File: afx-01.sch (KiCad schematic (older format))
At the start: 21 parts, among them P1 CONN_02X05, P2 CONN_02X08, Q5 BSS138, Q6 BSS138, U1 ADA_SSD1306_I2C, U10 MicroSD_Connector, U2 Teensy_3.1, U4 MicroSD_Adapter, U5 MCP1703

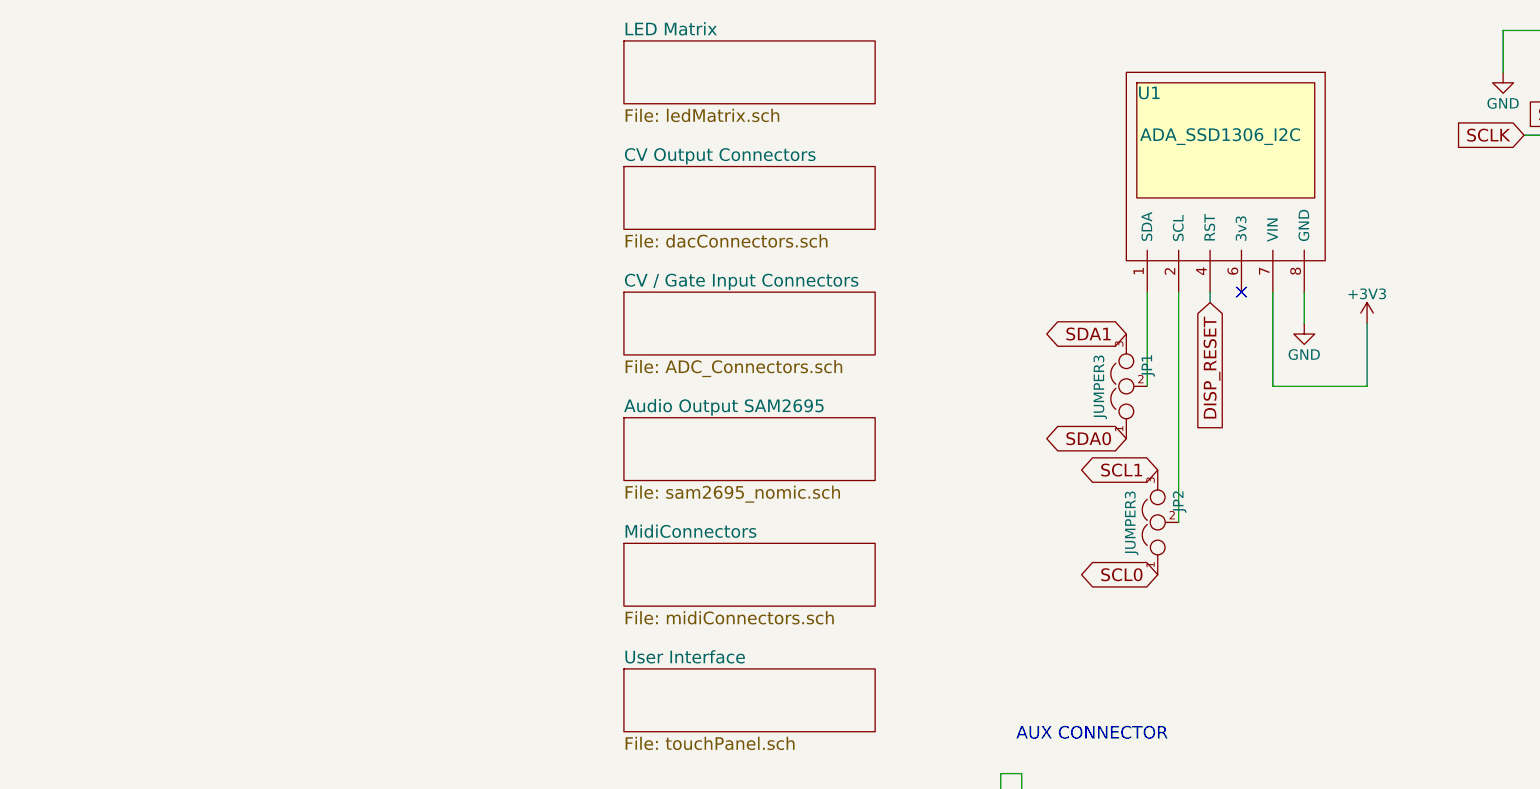
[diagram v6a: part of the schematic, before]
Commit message: UPDATING SCHEMATIC FOR SSD1327
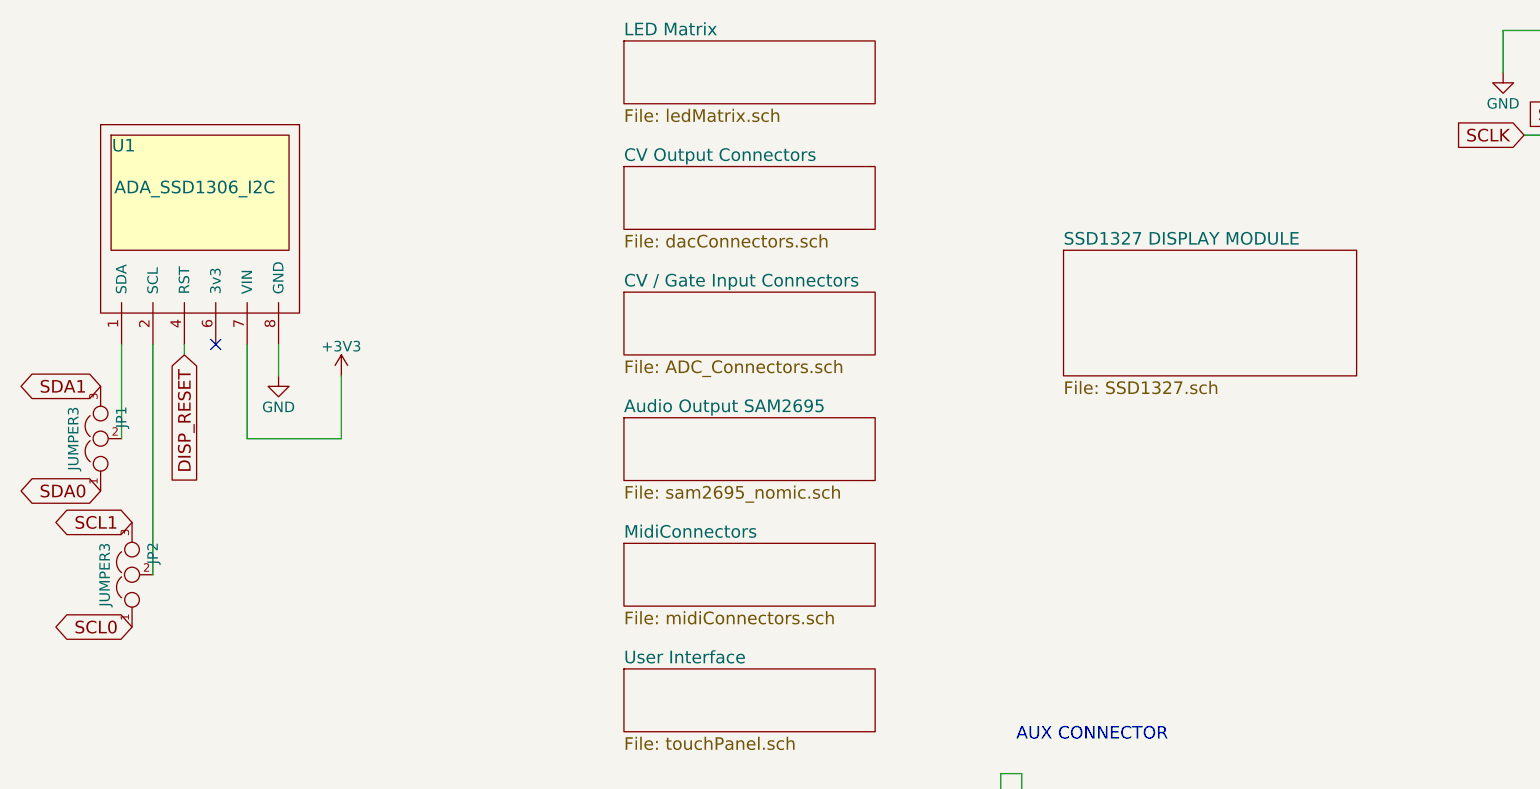
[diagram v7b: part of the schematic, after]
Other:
- moved on the sheet: JP1, JP2, U1
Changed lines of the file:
@@
 $Descr A4 11693 8268
 encoding utf-8
-Sheet 1 7
+Sheet 1 8
 Title ""
 Date ""
@@
 	0    -1   -1   0
 $EndComp
-NoConn ~ 3950 2000
+NoConn ~ -950 2250
 $Comp
 L ADA_SSD1306_I2C U1
 U 1 1 558492E1
-P 3850 1600
-F 0 "U1" H 3510 2150 60  0000 C CNN
-F 1 "ADA_SSD1306_I2C" H 3850 1950 60  0000 C CNN
-F 2 "Pin_Headers:Pin_Header_Straight_1x06" V 4050 1550 60  0001 C CNN
-F 3 "" V 4050 1550 60  0000 C CNN
-	1    3850 1600
+P -1050 1850
+F 0 "U1" H -1390 2400 60  0000 C CNN
+F 1 "ADA_SSD1306_I2C" H -1050 2200 60  0000 C CNN
+F 2 "Pin_Headers:Pin_Header_Straight_1x06" V -850 1800 60  0001 C CNN
+F 3 "" V -850 1800 60  0000 C CNN
+	1    -1050 1850
 	1    0    0    -1
 $EndComp
@@
 SD_CS
 $Comp
-L +3V3 #PWR17
+L +3V3 #PWR01
 U 1 1 561E6C12
 P 6800 5200
-F 0 "#PWR17" H 6800 5050 50  0001 C CNN
+F 0 "#PWR01" H 6800 5050 50  0001 C CNN
 F 1 "+3V3" H 6800 5340 50  0000 C CNN
 F 2 "" H 6800 5200 60  0000 C CNN
@@
 SCL1
 $Comp
-L +3V3 #PWR19
+L +3V3 #PWR02
 U 1 1 561E70C9
 P 10650 5200
-F 0 "#PWR19" H 10650 5050 50  0001 C CNN
+F 0 "#PWR02" H 10650 5050 50  0001 C CNN
 F 1 "+3V3" H 10650 5340 50  0000 C CNN
 F 2 "" H 10650 5200 60  0000 C CNN
@@
 Text GLabel 9900 3000 2    60   BiDi ~ 0
 SCL0
-Text GLabel 3400 2200 0    60   BiDi ~ 0
+Text GLabel -1500 2450 0    60   BiDi ~ 0
 SDA1
-Text GLabel 3550 2850 0    60   BiDi ~ 0
+Text GLabel -1350 3100 0    60   BiDi ~ 0
 SCL1
 Text GLabel 8600 4200 3    60   BiDi ~ 0
@@
 ENC1B
 $Comp
-L +3V3 #PWR12
+L +3V3 #PWR03
 U 1 1 561E88DC
 P 9300 3950
-F 0 "#PWR12" H 9300 3800 50  0001 C CNN
+F 0 "#PWR03" H 9300 3800 50  0001 C CNN
 F 1 "+3V3" H 9300 4090 50  0000 C CNN
 F 2 "" H 9300 3950 60  0000 C CNN
@@
 $EndComp
 $Comp
-L GND #PWR13
+L GND #PWR04
 U 1 1 561E894C
 P 9000 4050
-F 0 "#PWR13" H 9000 3800 50  0001 C CNN
+F 0 "#PWR04" H 9000 3800 50  0001 C CNN
 F 1 "GND" H 9000 3900 50  0000 C CNN
 F 2 "" H 9000 4050 60  0000 C CNN
@@
 $EndComp
 $Comp
-L +5V #PWR10
+L +5V #PWR05
 U 1 1 561E8C0A
 P 9500 2150
-F 0 "#PWR10" H 9500 2000 50  0001 C CNN
+F 0 "#PWR05" H 9500 2000 50  0001 C CNN
 F 1 "+5V" H 9500 2290 50  0000 C CNN
 F 2 "" H 9500 2150 60  0000 C CNN
@@
 $EndComp
 $Comp
-L +3V3 #PWR11
+L +3V3 #PWR06
 U 1 1 561E8F33
 P 9950 2400
-F 0 "#PWR11" H 9950 2250 50  0001 C CNN
+F 0 "#PWR06" H 9950 2250 50  0001 C CNN
 F 1 "+3V3" H 9950 2540 50  0000 C CNN
 F 2 "" H 9950 2400 60  0000 C CNN
@@
 $EndComp
 $Comp
-L GNDA #PWR7
+L GNDA #PWR07
 U 1 1 561E8FA3
 P 9800 2000
-F 0 "#PWR7" H 9800 1750 50  0001 C CNN
+F 0 "#PWR07" H 9800 1750 50  0001 C CNN
 F 1 "GNDA" H 9800 1850 50  0000 C CNN
 F 2 "" H 9800 2000 60  0000 C CNN
@@
 SCLK
 $Comp
-L GND #PWR6
+L GND #PWR08
 U 1 1 561E9F99
 P 9250 1800
-F 0 "#PWR6" H 9250 1550 50  0001 C CNN
+F 0 "#PWR08" H 9250 1550 50  0001 C CNN
 F 1 "GND" H 9250 1650 50  0000 C CNN
 F 2 "" H 9250 1800 60  0000 C CNN
@@
 $EndComp
 $Comp
-L GND #PWR5
+L GND #PWR09
 U 1 1 561EA0E7
 P 7550 1800
-F 0 "#PWR5" H 7550 1550 50  0001 C CNN
+F 0 "#PWR09" H 7550 1550 50  0001 C CNN
 F 1 "GND" H 7550 1650 50  0000 C CNN
 F 2 "" H 7550 1800 60  0000 C CNN
@@
 SCLK
 $Comp
-L GND #PWR1
+L GND #PWR010
 U 1 1 561EAAFA
 P 5200 950
-F 0 "#PWR1" H 5200 700 50  0001 C CNN
+F 0 "#PWR010" H 5200 700 50  0001 C CNN
 F 1 "GND" H 5200 800 50  0000 C CNN
 F 2 "" H 5200 950 60  0000 C CNN
@@
 MOSI
 $Comp
-L +5V #PWR4
+L +5V #PWR011
 U 1 1 561EAD75
 P 6950 1600
-F 0 "#PWR4" H 6950 1450 50  0001 C CNN
+F 0 "#PWR011" H 6950 1450 50  0001 C CNN
 F 1 "+5V" H 6950 1740 50  0000 C CNN
 F 2 "" H 6950 1600 60  0000 C CNN
@@
 Text GLabel 6650 2900 0    60   Output ~ 0
 DISP_RESET
-Text GLabel 3800 2050 3    60   Input ~ 0
+Text GLabel -1100 2300 3    60   Input ~ 0
 DISP_RESET
 $Comp
-L GND #PWR8
+L GND #PWR012
 U 1 1 561EB8E2
-P 4250 2150
-F 0 "#PWR8" H 4250 1900 50  0001 C CNN
-F 1 "GND" H 4250 2000 50  0000 C CNN
-F 2 "" H 4250 2150 60  0000 C CNN
-F 3 "" H 4250 2150 60  0000 C CNN
-	1    4250 2150
-	1    0    0    -1
-$EndComp
-$Comp
-L +3V3 #PWR9
+P -650 2400
+F 0 "#PWR012" H -650 2150 50  0001 C CNN
+F 1 "GND" H -650 2250 50  0000 C CNN
+F 2 "" H -650 2400 60  0000 C CNN
+F 3 "" H -650 2400 60  0000 C CNN
+	1    -650 2400
+	1    0    0    -1
+$EndComp
+$Comp
+L +3V3 #PWR013
 U 1 1 561EBA2E
-P 4550 2150
-F 0 "#PWR9" H 4550 2000 50  0001 C CNN
-F 1 "+3V3" H 4550 2290 50  0000 C CNN
-F 2 "" H 4550 2150 60  0000 C CNN
-F 3 "" H 4550 2150 60  0000 C CNN
-	1    4550 2150
+P -350 2400
+F 0 "#PWR013" H -350 2250 50  0001 C CNN
+F 1 "+3V3" H -350 2540 50  0000 C CNN
+F 2 "" H -350 2400 60  0000 C CNN
+F 3 "" H -350 2400 60  0000 C CNN
+	1    -350 2400
 	1    0    0    -1
 $EndComp
@@
 LED_DIN
 $Comp
-L GND #PWR14
+L GND #PWR014
 U 1 1 561EC8D9
 P 2800 4400
-F 0 "#PWR14" H 2800 4150 50  0001 C CNN
+F 0 "#PWR014" H 2800 4150 50  0001 C CNN
 F 1 "GND" H 2800 4250 50  0000 C CNN
 F 2 "" H 2800 4400 60  0000 C CNN
@@
 $EndComp
 $Comp
-L +3V3 #PWR15
+L +3V3 #PWR015
 U 1 1 561EC92C
 P 2550 4550
-F 0 "#PWR15" H 2550 4400 50  0001 C CNN
+F 0 "#PWR015" H 2550 4400 50  0001 C CNN
 F 1 "+3V3" H 2550 4690 50  0000 C CNN
 F 2 "" H 2550 4550 60  0000 C CNN
@@
 $EndComp
 $Comp
-L +5V #PWR16
+L +5V #PWR016
 U 1 1 561EC97F
 P 2300 4700
-F 0 "#PWR16" H 2300 4550 50  0001 C CNN
+F 0 "#PWR016" H 2300 4550 50  0001 C CNN
 F 1 "+5V" H 2300 4840 50  0000 C CNN
 F 2 "" H 2300 4700 60  0000 C CNN
@@
 SCLK
 $Comp
-L VDD #PWR20
+L VDD #PWR017
 U 1 1 561ED246
 P 2000 5600
-F 0 "#PWR20" H 2000 5450 50  0001 C CNN
+F 0 "#PWR017" H 2000 5450 50  0001 C CNN
 F 1 "VDD" H 2000 5750 50  0000 C CNN
 F 2 "" H 2000 5600 60  0000 C CNN
@@
 $EndComp
 $Comp
-L VSS #PWR25
+L VSS #PWR018
 U 1 1 561ED2BD
 P 2000 7000
-F 0 "#PWR25" H 2000 6850 50  0001 C CNN
+F 0 "#PWR018" H 2000 6850 50  0001 C CNN
 F 1 "VSS" H 2000 7150 50  0000 C CNN
 F 2 "" H 2000 7000 60  0000 C CNN
@@
 $EndComp
 $Comp
-L GND #PWR22
+L GND #PWR019
 U 1 1 561ED883
 P 1250 6200
-F 0 "#PWR22" H 1250 5950 50  0001 C CNN
+F 0 "#PWR019" H 1250 5950 50  0001 C CNN
 F 1 "GND" H 1250 6050 50  0000 C CNN
 F 2 "" H 1250 6200 60  0000 C CNN
@@
 $EndComp
 $Comp
-L GND #PWR23
+L GND #PWR020
 U 1 1 561ED8D9
 P 2750 6200
-F 0 "#PWR23" H 2750 5950 50  0001 C CNN
+F 0 "#PWR020" H 2750 5950 50  0001 C CNN
 F 1 "GND" H 2750 6050 50  0000 C CNN
 F 2 "" H 2750 6200 60  0000 C CNN
@@
 $EndComp
 $Comp
-L GND #PWR26
+L GND #PWR021
 U 1 1 5620975C
 P 4400 7050
-F 0 "#PWR26" H 4400 6800 50  0001 C CNN
+F 0 "#PWR021" H 4400 6800 50  0001 C CNN
 F 1 "GND" H 4400 6900 50  0000 C CNN
 F 2 "" H 4400 7050 60  0000 C CNN
@@
 $EndComp
 $Comp
-L VDD #PWR24
+L VDD #PWR022
 U 1 1 562097B5
 P 5100 6300
-F 0 "#PWR24" H 5100 6150 50  0001 C CNN
+F 0 "#PWR022" H 5100 6150 50  0001 C CNN
 F 1 "VDD" H 5100 6450 50  0000 C CNN
 F 2 "" H 5100 6300 60  0000 C CNN
@@
 $EndComp
 $Comp
-L +5V #PWR21
+L +5V #PWR023
 U 1 1 5620980E
 P 3300 5950
-F 0 "#PWR21" H 3300 5800 50  0001 C CNN
+F 0 "#PWR023" H 3300 5800 50  0001 C CNN
 F 1 "+5V" H 3300 6090 50  0000 C CNN
 F 2 "" H 3300 5950 60  0000 C CNN
@@
 L JUMPER3 JP1
 U 1 1 5621F7E9
-P 3400 2450
-F 0 "JP1" H 3450 2350 50  0000 L CNN
-F 1 "JUMPER3" H 3400 2550 50  0000 C BNN
-F 2 "Zetaohm:Jumper_3way" H 3400 2450 60  0001 C CNN
-F 3 "" H 3400 2450 60  0000 C CNN
-	1    3400 2450
+P -1500 2700
+F 0 "JP1" H -1450 2600 50  0000 L CNN
+F 1 "JUMPER3" H -1500 2800 50  0000 C BNN
+F 2 "Zetaohm:Jumper_3way" H -1500 2700 60  0001 C CNN
+F 3 "" H -1500 2700 60  0000 C CNN
+	1    -1500 2700
 	0    -1   -1   0
 $EndComp
-Text GLabel 3400 2700 0    60   BiDi ~ 0
+Text GLabel -1500 2950 0    60   BiDi ~ 0
 SDA0
 $Comp
 L JUMPER3 JP2
 U 1 1 5621FB71
-P 3550 3100
-F 0 "JP2" H 3600 3000 50  0000 L CNN
-F 1 "JUMPER3" H 3550 3200 50  0000 C BNN
-F 2 "Zetaohm:Jumper_3way" H 3550 3100 60  0001 C CNN
-F 3 "" H 3550 3100 60  0000 C CNN
-	1    3550 3100
+P -1350 3350
+F 0 "JP2" H -1300 3250 50  0000 L CNN
+F 1 "JUMPER3" H -1350 3450 50  0000 C BNN
+F 2 "Zetaohm:Jumper_3way" H -1350 3350 60  0001 C CNN
+F 3 "" H -1350 3350 60  0000 C CNN
+	1    -1350 3350
 	0    -1   -1   0
 $EndComp
-Text GLabel 3550 3350 0    60   BiDi ~ 0
+Text GLabel -1350 3600 0    60   BiDi ~ 0
 SCL0
 $Sheet
@@
 $EndComp
 $Comp
-L +5V #PWR18
+L +5V #PWR024
 U 1 1 56228B3B
 P 8750 5200
-F 0 "#PWR18" H 8750 5050 50  0001 C CNN
+F 0 "#PWR024" H 8750 5050 50  0001 C CNN
 F 1 "+5V" H 8750 5340 50  0000 C CNN
 F 2 "" H 8750 5200 60  0000 C CNN
@@
 SCLK
 $Comp
-L +3V3 #PWR3
+L +3V3 #PWR025
 U 1 1 56235638
 P 7900 1250
-F 0 "#PWR3" H 7900 1100 50  0001 C CNN
+F 0 "#PWR025" H 7900 1100 50  0001 C CNN
 F 1 "+3V3" H 7900 1390 50  0000 C CNN
 F 2 "" H 7900 1250 60  0000 C CNN
@@
 $EndComp
 $Comp
-L GND #PWR2
+L GND #PWR026
 U 1 1 562356B5
 P 10000 1200
-F 0 "#PWR2" H 10000 950 50  0001 C CNN
+F 0 "#PWR026" H 10000 950 50  0001 C CNN
 F 1 "GND" H 10000 1050 50  0000 C CNN
 F 2 "" H 10000 1200 60  0000 C CNN
@@
 	6750 1750 6950 1750
 Wire Wire Line
-	4100 2000 4100 2450
-Wire Wire Line
-	3800 2000 3800 2050
+	-800 2250 -800 2700
+Wire Wire Line
+	-1100 2250 -1100 2300
 Wire Wire Line
 	6800 5200 6800 5550
@@
 	6950 1750 6950 1600
 Wire Wire Line
-	3500 2000 3500 2450
-Wire Wire Line
-	3650 2000 3650 3100
-Wire Wire Line
-	4250 2000 4250 2150
-Wire Wire Line
-	4100 2450 4550 2450
-Wire Wire Line
-	4550 2450 4550 2150
+	-1400 2250 -1400 2700
+Wire Wire Line
+	-1250 2250 -1250 3350
+Wire Wire Line
+	-650 2250 -650 2400
+Wire Wire Line
+	-800 2700 -350 2700
+Wire Wire Line
+	-350 2700 -350 2400
 Wire Wire Line
 	7700 2900 6650 2900
@@
 PIN_A0
 NoConn ~ 7450 2400
+$Sheet
+S 3100 1800 1400 600
+U 562AF5FF
+F0 "SSD1327 DISPLAY MODULE" 60
+F1 "SSD1327.sch" 60
+$EndSheet
 $EndSCHEMATC
